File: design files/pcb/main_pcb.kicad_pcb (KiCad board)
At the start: 2 copper layers, 29 x 99.8 mm, 26 parts, among them J1 O1, J2 O5, J3 O2, J4 O6, J5 O3, J6 O4, J7 CLK

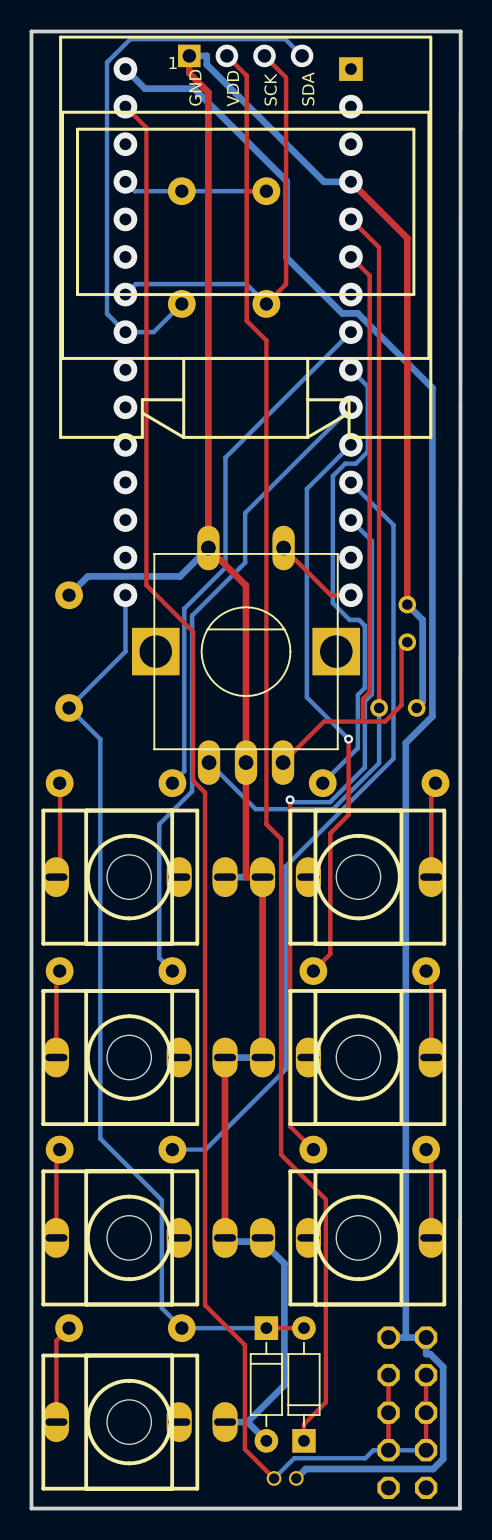
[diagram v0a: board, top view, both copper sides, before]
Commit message: new symmetric pcb and panel
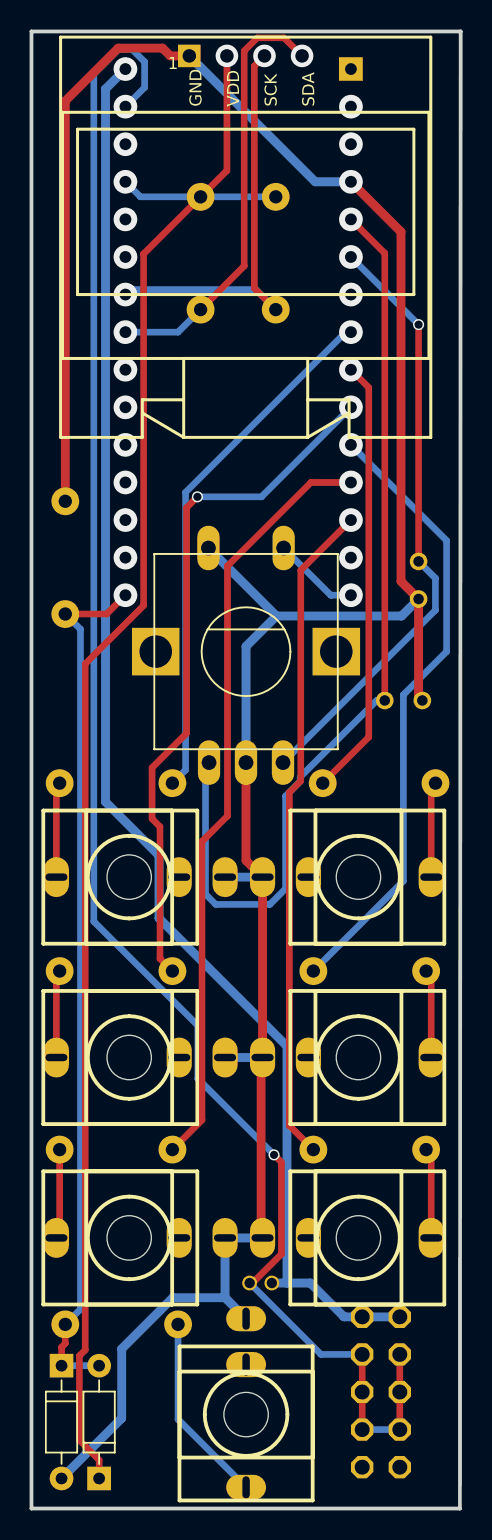
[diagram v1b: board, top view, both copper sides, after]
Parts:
- moved D1 14.1 mm to (9.65, 196.5)
- moved D2 14.1 mm to (7.11, 196.5)
- moved C3 13.3 mm to (20.6, 187.1)
- moved J7 7.92 mm to (19.6, 196.0), turned to 180 degrees
- moved R10 6.36 mm to (7.37, 138.0)
- moved C1 3.02 mm to (31.2, 139.6), turned to -90 degrees
- moved EP1 2.26 mm to (28.7, 194.4)
- moved R7 1.33 mm to (16.5, 117.5)
- moved R8 0.74 mm to (21.6, 117.5)
- moved C2 0.64 mm to (30.2, 147.7)
- moved R9 0.36 mm to (11.2, 189.9), turned to 180 degrees
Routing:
- net 12V: track 119.5 -> 97.3 mm
- net C2_1: track 51.6 -> 64.4 mm
- net GND: track 170.5 -> 181.1 mm
- net SDA: track 37.6 -> 29.2 mm
- net R9_2: track 6.70 -> 12.9 mm
- net C1_2: track 46.1 -> 40.8 mm, vias 1 -> 2
- net R10_1: track 62.5 -> 58.9 mm
- net ARD_5: track 108.1 -> 111.4 mm
- net O4: track 38.9 -> 42.0 mm, vias 2 -> 1
- net O6: track 47.9 -> 44.9 mm, vias 2 -> 1
- net O3: track 43.8 -> 46.8 mm, vias 1 -> 2
- net O2: track 32.3 -> 29.7 mm
- net O5: track 53.8 -> 51.7 mm
- net SCL: track 28.3 -> 28.9 mm
- net EP1_GND0: track 118.1 -> 118.3 mm, vias 1 -> 2
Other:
- board text added: "Arduino nano"
- board text added: "USB here"
- board text removed: "REF"

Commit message: bigger resistors
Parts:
- R1, R2, R3, R4, R5, R6, R9: value 470 -> 2.2k
